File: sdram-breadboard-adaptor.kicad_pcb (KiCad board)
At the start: 2 copper layers, 6 parts, among them J1 Conn_01x40, J2 Conn_01x40, U1 LY62W10248ML-55LLI, U2 LY62W10248ML-55LLI, U3 LY62W10248ML-55LLI, U4 LY62W10248ML-55LLI

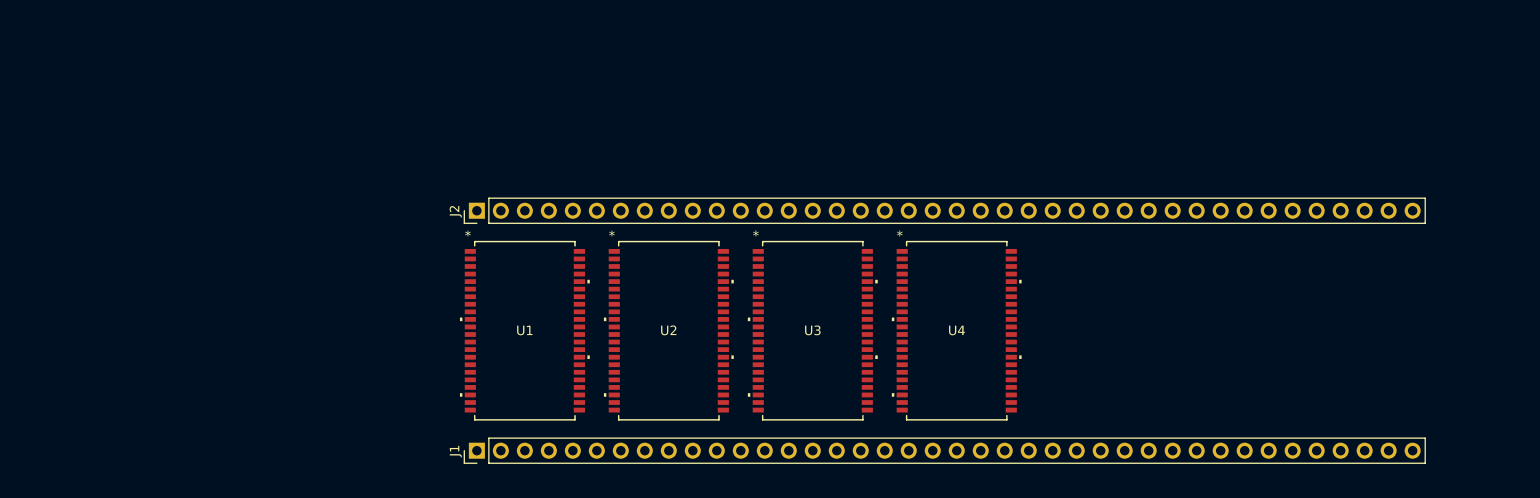
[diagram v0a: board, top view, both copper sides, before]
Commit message: add 4 more chips
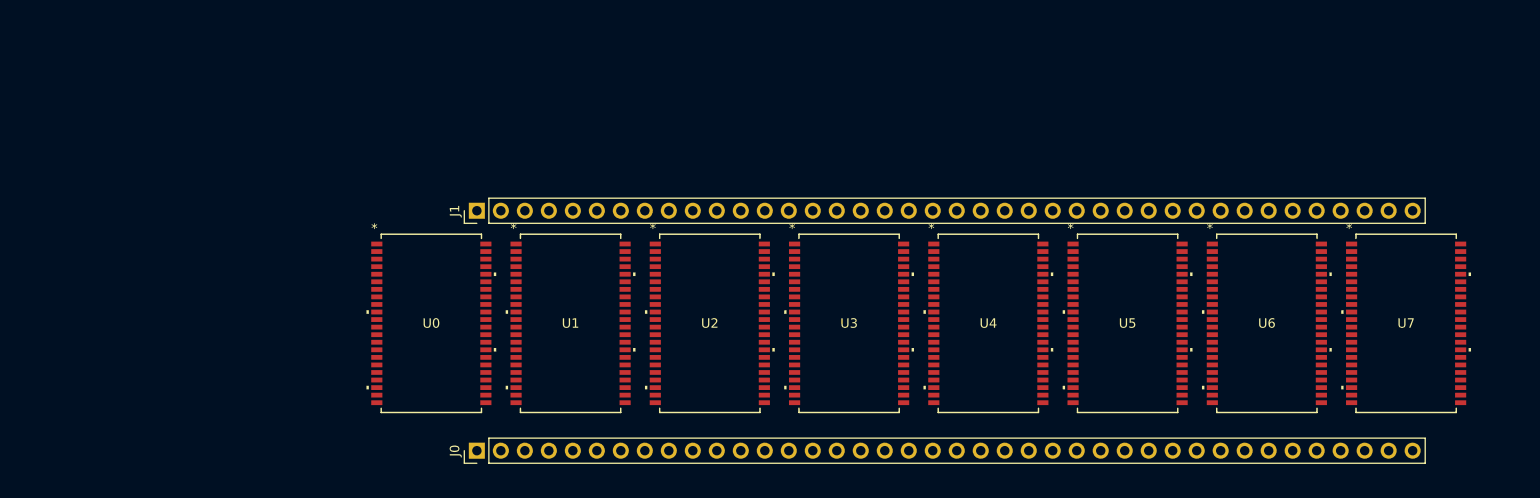
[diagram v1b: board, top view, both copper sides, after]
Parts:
- added U0: LY62W10248ML-55LLI, TSOP-II 44:TSOP-II-44_400MIL_LTK, F.Cu at (96.8, 85.6)
- added U5: LY62W10248ML-55LLI, TSOP-II 44:TSOP-II-44_400MIL_LTK, F.Cu at (170.5, 85.6)
- added U6: LY62W10248ML-55LLI, TSOP-II 44:TSOP-II-44_400MIL_LTK, F.Cu at (185.2, 85.6)
- added U7: LY62W10248ML-55LLI, TSOP-II 44:TSOP-II-44_400MIL_LTK, F.Cu at (200.0, 85.6)
- moved U1 4.90 mm to (111.5, 85.6)
- moved U2 4.41 mm to (126.3, 85.6)
- moved U3 3.92 mm to (141.0, 85.6)
- moved U4 3.43 mm to (155.7, 85.6)
- renumbered J1 to J0, J2 to J1
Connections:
- J0 pad 1: unconnected-(J1-Pin_1-Pad1) -> +5V
- J0 pad 22: unconnected-(J1-Pin_22-Pad22) -> GND
- J0 pad 23: unconnected-(J1-Pin_23-Pad23) -> /R/W
- J0 pad 24: unconnected-(J1-Pin_24-Pad24) -> /~{CEA0}
- J0 pad 25: unconnected-(J1-Pin_25-Pad25) -> /~{CEA1}
- J0 pad 26: unconnected-(J1-Pin_26-Pad26) -> /~{CEA2}
- J0 pad 27: unconnected-(J1-Pin_27-Pad27) -> /~{CEA3}
- J0 pad 28: unconnected-(J1-Pin_28-Pad28) -> /~{CEB0}
- J0 pad 29: unconnected-(J1-Pin_29-Pad29) -> /~{CEB1}
- J0 pad 30: unconnected-(J1-Pin_30-Pad30) -> /~{CEB2}
- J0 pad 31: unconnected-(J1-Pin_31-Pad31) -> /~{CEB3}
- J0 pad 40: unconnected-(J1-Pin_40-Pad40) -> GND
- J1 pad 1: unconnected-(J2-Pin_1-Pad1) -> GND
- J1 pad 10: unconnected-(J2-Pin_10-Pad10) -> /D29
- J1 pad 11: unconnected-(J2-Pin_11-Pad11) -> /D28
- J1 pad 12: unconnected-(J2-Pin_12-Pad12) -> /D27
- J1 pad 13: unconnected-(J2-Pin_13-Pad13) -> /D26
- J1 pad 14: unconnected-(J2-Pin_14-Pad14) -> /D25
- J1 pad 15: unconnected-(J2-Pin_15-Pad15) -> /D24
- J1 pad 16: unconnected-(J2-Pin_16-Pad16) -> /D23
- J1 pad 17: unconnected-(J2-Pin_17-Pad17) -> /D22
- J1 pad 18: unconnected-(J2-Pin_18-Pad18) -> /D21
- J1 pad 19: unconnected-(J2-Pin_19-Pad19) -> /D20
- J1 pad 20: unconnected-(J2-Pin_20-Pad20) -> /D19
- J1 pad 21: unconnected-(J2-Pin_21-Pad21) -> /D18
- J1 pad 22: unconnected-(J2-Pin_22-Pad22) -> /D17
- J1 pad 23: unconnected-(J2-Pin_23-Pad23) -> /D16
- J1 pad 24: unconnected-(J2-Pin_24-Pad24) -> /D15
- J1 pad 25: unconnected-(J2-Pin_25-Pad25) -> /D14
- J1 pad 26: unconnected-(J2-Pin_26-Pad26) -> /D13
- J1 pad 27: unconnected-(J2-Pin_27-Pad27) -> /D12
- J1 pad 28: unconnected-(J2-Pin_28-Pad28) -> /D11
- J1 pad 29: unconnected-(J2-Pin_29-Pad29) -> /D10
- J1 pad 30: unconnected-(J2-Pin_30-Pad30) -> /D9
- J1 pad 31: unconnected-(J2-Pin_31-Pad31) -> /D8
- J1 pad 32: unconnected-(J2-Pin_32-Pad32) -> /D7
- J1 pad 33: unconnected-(J2-Pin_33-Pad33) -> /D6
- J1 pad 34: unconnected-(J2-Pin_34-Pad34) -> /D5
- J1 pad 35: unconnected-(J2-Pin_35-Pad35) -> /D4
- J1 pad 36: unconnected-(J2-Pin_36-Pad36) -> /D3
- J1 pad 37: unconnected-(J2-Pin_37-Pad37) -> /D2
- J1 pad 38: unconnected-(J2-Pin_38-Pad38) -> /D1
- J1 pad 39: unconnected-(J2-Pin_39-Pad39) -> /D0
- J1 pad 40: unconnected-(J2-Pin_40-Pad40) -> +5V
- J1 pad 8: unconnected-(J2-Pin_8-Pad8) -> /D31
- J1 pad 9: unconnected-(J2-Pin_9-Pad9) -> /D30
- U1 pad 10: /D1 -> /D9
- U1 pad 11: unconnected-(U1-VCC-Pad11) -> +5V
- U1 pad 12: unconnected-(U1-VSS-Pad12) -> GND
- U1 pad 13: /D2 -> /D10
- U1 pad 14: /D3 -> /D11
- U1 pad 17: unconnected-(U1-WE#-Pad17) -> /R/W
- U1 pad 31: /D4 -> /D12
- U1 pad 32: /D5 -> /D13
- U1 pad 33: unconnected-(U1-VCC-Pad33) -> +5V
- U1 pad 34: unconnected-(U1-VSS-Pad34) -> GND
- U1 pad 35: /D6 -> /D14
- U1 pad 36: /D7 -> /D15
- U1 pad 40: unconnected-(U1-CE2-Pad40) -> +5V
- U1 pad 41: unconnected-(U1-OE#-Pad41) -> GND
- U1 pad 6: unconnected-(U1-CE#-Pad6) -> /~{CEA1}
- U1 pad 9: /D0 -> /D8
- U2 pad 10: /D9 -> /D17
- U2 pad 11: unconnected-(U2-VCC-Pad11) -> +5V
- U2 pad 12: unconnected-(U2-VSS-Pad12) -> GND
- U2 pad 13: /D10 -> /D18
- U2 pad 14: /D11 -> /D19
- U2 pad 17: unconnected-(U2-WE#-Pad17) -> /R/W
- U2 pad 31: /D12 -> /D20
- U2 pad 32: /D13 -> /D21
- U2 pad 33: unconnected-(U2-VCC-Pad33) -> +5V
- U2 pad 34: unconnected-(U2-VSS-Pad34) -> GND
- U2 pad 35: /D14 -> /D22
- U2 pad 36: /D15 -> /D23
- U2 pad 40: unconnected-(U2-CE2-Pad40) -> +5V
- U2 pad 41: unconnected-(U2-OE#-Pad41) -> GND
- U2 pad 6: unconnected-(U2-CE#-Pad6) -> /~{CEA2}
- U2 pad 9: /D8 -> /D16
- U3 pad 10: /D17 -> /D25
- U3 pad 11: unconnected-(U3-VCC-Pad11) -> +5V
- U3 pad 12: unconnected-(U3-VSS-Pad12) -> GND
- U3 pad 13: /D18 -> /D26
- U3 pad 14: /D19 -> /D27
- U3 pad 17: unconnected-(U3-WE#-Pad17) -> /R/W
- U3 pad 31: /D20 -> /D28
- U3 pad 32: /D21 -> /D29
- U3 pad 33: unconnected-(U3-VCC-Pad33) -> +5V
- U3 pad 34: unconnected-(U3-VSS-Pad34) -> GND
- U3 pad 35: /D22 -> /D30
- U3 pad 36: /D23 -> /D31
- U3 pad 40: unconnected-(U3-CE2-Pad40) -> +5V
- U3 pad 41: unconnected-(U3-OE#-Pad41) -> GND
- U3 pad 6: unconnected-(U3-CE#-Pad6) -> /~{CEA3}
- U3 pad 9: /D16 -> /D24
- U4 pad 10: /D25 -> /D1
- U4 pad 11: unconnected-(U4-VCC-Pad11) -> +5V
- U4 pad 12: unconnected-(U4-VSS-Pad12) -> GND
- U4 pad 13: /D26 -> /D2
- U4 pad 14: /D27 -> /D3
- U4 pad 17: unconnected-(U4-WE#-Pad17) -> /R/W
- U4 pad 31: /D28 -> /D4
- U4 pad 32: /D29 -> /D5
- U4 pad 33: unconnected-(U4-VCC-Pad33) -> +5V
- U4 pad 34: unconnected-(U4-VSS-Pad34) -> GND
- U4 pad 35: /D30 -> /D6
- U4 pad 36: /D31 -> /D7
- U4 pad 40: unconnected-(U4-CE2-Pad40) -> +5V
- U4 pad 41: unconnected-(U4-OE#-Pad41) -> GND
- U4 pad 6: unconnected-(U4-CE#-Pad6) -> /~{CEB0}
- U4 pad 9: /D24 -> /D0

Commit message: add silkscreen
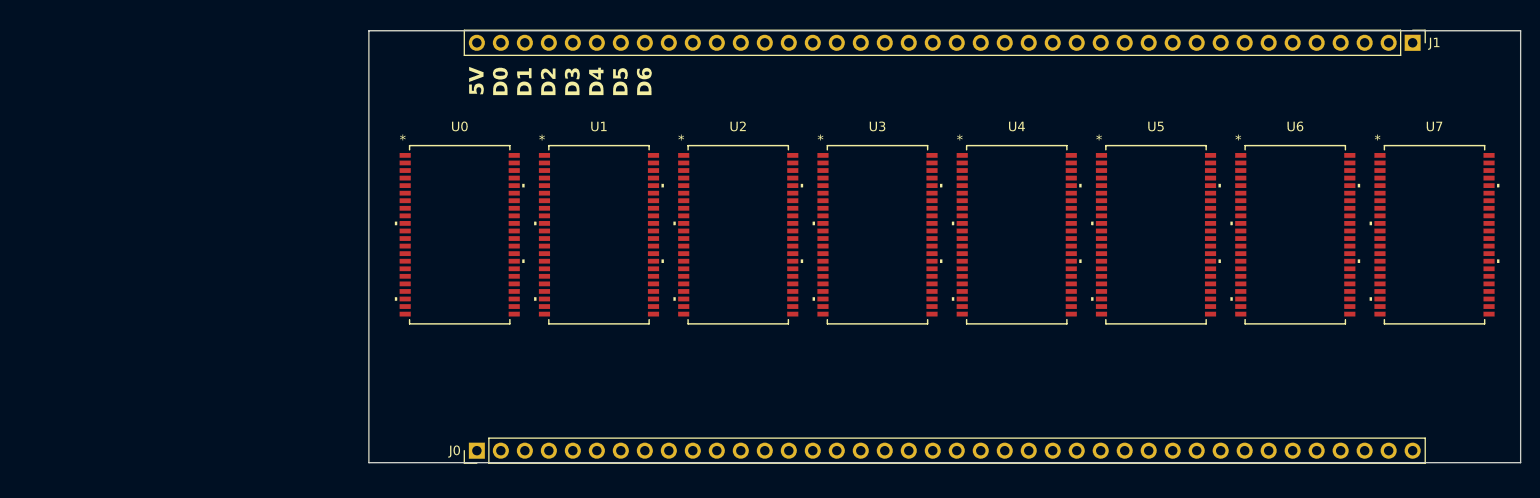
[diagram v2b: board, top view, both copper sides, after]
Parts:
- moved J1 100.6 mm to (200.7, 55.9), turned to -90 degrees
- moved U0 9.85 mm to (99.8, 76.2)
- moved U1 9.85 mm to (114.5, 76.2)
- moved U2 9.85 mm to (129.3, 76.2)
- moved U3 9.85 mm to (144.0, 76.2)
- moved U4 9.85 mm to (158.8, 76.2)
- moved U5 9.85 mm to (173.5, 76.2)
- moved U6 9.85 mm to (188.2, 76.2)
- moved U7 9.85 mm to (203.0, 76.2)
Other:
- board outline added: 121.9 x 45.7 mm
- board text added: "5V"
- board text added: "D0"
- board text added: "D1"
- board text added: "D2"
- board text added: "D3"
- board text added: "D4"
- board text added: "D5"
- board text added: "D6"

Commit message: add data bus connections
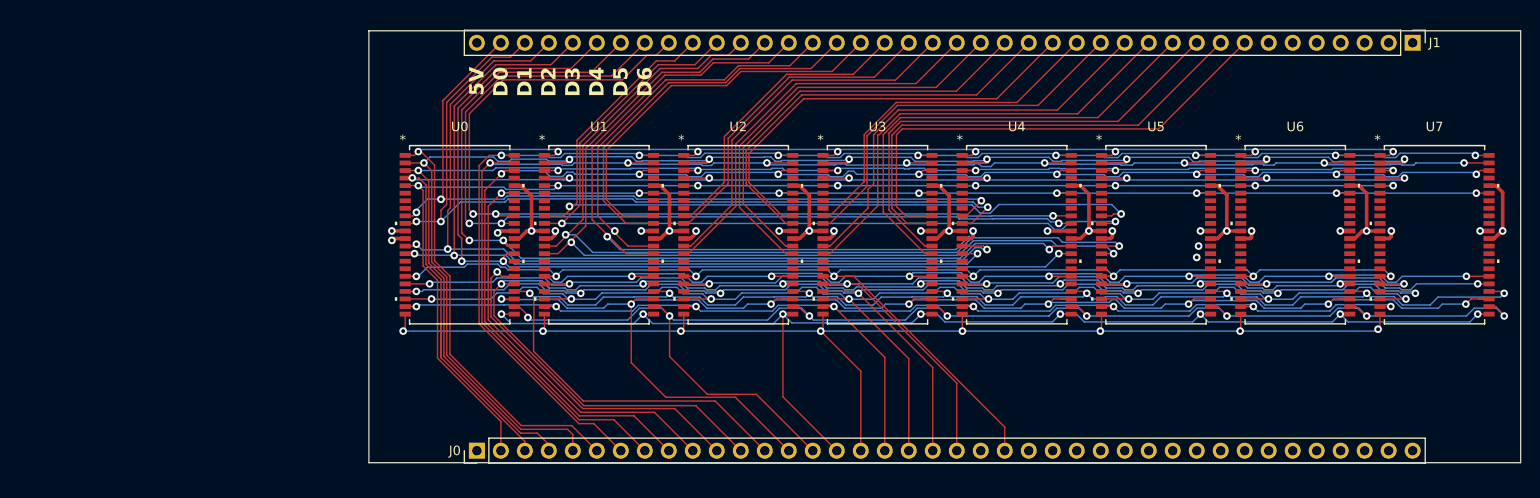
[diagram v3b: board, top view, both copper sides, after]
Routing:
- net /A5: track 0.00 -> 183.8 mm, vias 0 -> 8
- net /A8: track 0.00 -> 166.1 mm, vias 0 -> 8
- net /A20: track 0.00 -> 165.1 mm, vias 0 -> 8
- net /A3: track 0.00 -> 160.7 mm, vias 0 -> 8
- net /A6: track 0.00 -> 160.4 mm, vias 0 -> 8
- net /A14: track 0.00 -> 158.9 mm, vias 0 -> 8
- net /A13: track 0.00 -> 158.2 mm, vias 0 -> 8
- net /A9: track 0.00 -> 157.5 mm, vias 0 -> 8
- net /A10: track 0.00 -> 156.4 mm, vias 0 -> 8
- net /A11: track 0.00 -> 156.1 mm, vias 0 -> 8
- net /A7: track 0.00 -> 155.8 mm, vias 0 -> 8
- net /A12: track 0.00 -> 154.6 mm, vias 0 -> 8
- net /A4: track 0.00 -> 152.6 mm, vias 0 -> 8
- net /A19: track 0.00 -> 152.0 mm, vias 0 -> 8
- net /A21: track 0.00 -> 151.2 mm, vias 0 -> 8
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- added copper zone on In1.Cu, net +5V
- added copper zone on In2.Cu, net GND
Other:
- copper layers 2 -> 4

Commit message: add bypass caps
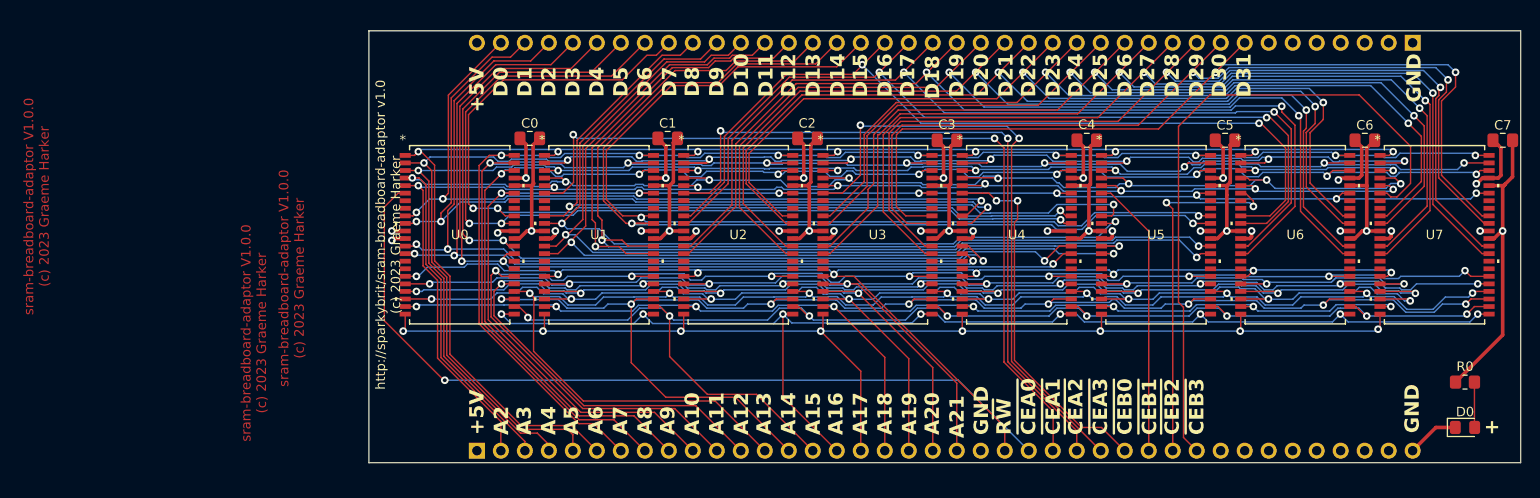
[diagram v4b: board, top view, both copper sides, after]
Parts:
- added C0: 100nF, Capacitor_SMD:C_0805_2012Metric_Pad1.18x1.45mm_HandSolder, F.Cu at (107.2, 66.0)
- added C1: 110nF, Capacitor_SMD:C_0805_2012Metric_Pad1.18x1.45mm_HandSolder, F.Cu at (121.8, 66.0)
- added C2: 100nF, Capacitor_SMD:C_0805_2012Metric_Pad1.18x1.45mm_HandSolder, F.Cu at (136.6, 66.0)
- added C3: 100nF, Capacitor_SMD:C_0805_2012Metric_Pad1.18x1.45mm_HandSolder, F.Cu at (151.4, 66.2)
- added C4: 100nF, Capacitor_SMD:C_0805_2012Metric_Pad1.18x1.45mm_HandSolder, F.Cu at (166.2, 66.2)
- added C5: 100nF, Capacitor_SMD:C_0805_2012Metric_Pad1.18x1.45mm_HandSolder, F.Cu at (180.8, 66.2)
- added C6: 100nF, Capacitor_SMD:C_0805_2012Metric_Pad1.18x1.45mm_HandSolder, F.Cu at (195.6, 66.2)
- added C7: 100nF, Capacitor_SMD:C_0805_2012Metric_Pad1.18x1.45mm_HandSolder, F.Cu at (210.2, 66.2)
- added D0: LED, LED_SMD:LED_0805_2012Metric_Pad1.15x1.40mm_HandSolder, F.Cu at (206.2, 96.6)
- added R0: 330R, Resistor_SMD:R_0805_2012Metric_Pad1.20x1.40mm_HandSolder, F.Cu at (206.2, 91.8)
- J0, J1: moved to B.Cu
- turned J0 to -90 degrees
- turned J1 to 90 degrees
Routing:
- net /~{CEA1}: track 0.00 -> 89.0 mm, vias 0 -> 2
- net /~{CEA0}: track 0.00 -> 88.8 mm, vias 0 -> 1
- net /~{CEA2}: track 0.00 -> 76.6 mm, vias 0 -> 2
- net /~{CEB3}: track 0.00 -> 71.7 mm
- net /D13: track 41.9 -> 108.6 mm
- net +5V: track 75.7 -> 140.8 mm
- net /~{CEA3}: track 0.00 -> 64.7 mm, vias 0 -> 2
- net /D14: track 41.2 -> 105.3 mm, vias 0 -> 2
- net /D15: track 42.6 -> 103.9 mm, vias 0 -> 2
- net /D16: track 31.7 -> 91.2 mm, vias 0 -> 2
- net /D17: track 34.6 -> 93.6 mm, vias 0 -> 2
- net /D18: track 39.3 -> 98.0 mm, vias 0 -> 2
- net /D19: track 42.0 -> 100.5 mm, vias 0 -> 2
- net /D20: track 44.2 -> 101.7 mm, vias 0 -> 2
- net /D21: track 45.3 -> 99.8 mm, vias 0 -> 2
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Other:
- board text added: "+"
- board text added: "+5V"
- board text added: "A10"
- board text added: "A11"
- board text added: "A12"
- board text added: "A13"
- board text added: "A14"
- board text added: "A15"
- board text added: "A16"
- board text added: "A17"
- board text added: "A18"
- board text added: "A19"
- board text added: "A2"
- board text added: "A20"
- board text added: "A21"
- board text added: "A3"
- board text added: "A4"
- board text added: "A5"
- board text added: "A6"
- board text added: "A7"
- board text added: "A8"
- board text added: "A9"
- board text added: "D10"
- board text added: "D11"
- board text added: "D12"
- board text added: "D13"
- board text added: "D14"
- board text added: "D15"
- board text added: "D16"
- board text added: "D17"
- board text added: "D18"
- board text added: "D19"
- board text added: "D20"
- board text added: "D21"
- board text added: "D22"
- board text added: "D23"
- board text added: "D24"
- board text added: "D25"
- board text added: "D26"
- board text added: "D27"
- board text added: "D28"
- board text added: "D29"
- board text added: "D30"
- board text added: "D31"
- board text added: "D7"
- board text added: "D8"
- board text added: "D9"
- board text added: "GND"
- board text added: "R~{W}"
- board text added: "http://sparkybrit/sram-breadboard-adaptor v1.0 (c) 2023 Graeme Harker"
- board text added: "sram-breadboard-adaptor V1.0.0 (c) 2023 Graeme Harker"
- board text added: "~{CEA0}"
- board text added: "~{CEA1}"
- board text added: "~{CEA2}"
- board text added: "~{CEA3}"
- board text added: "~{CEB0}"
- board text added: "~{CEB1}"
- board text added: "~{CEB2}"
- board text added: "~{CEB3}"
- board text removed: "5V"
